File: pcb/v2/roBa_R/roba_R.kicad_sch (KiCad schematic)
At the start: 50 parts, among them J2 Conn_01x01-Connector_Generic, J3 Conn_01x01-Connector_Generic, J4 Conn_01x01-Connector_Generic, J5 Conn_01x01-Connector_Generic, J6 Conn_01x01-Connector_Generic, J7 Conn_01x01-Connector_Generic, SW1 SW_PUSH, SW10 SW_PUSH, SW11 SW_PUSH, SW12 SW_PUSH, SW13 SW_PUSH, SW14 SW_PUSH, SW15 SW_PUSH, SW16 SW_PUSH, SW17 SW_PUSH, SW18 SW_PUSH, SW19 SW_PUSH, SW2 SW_PUSH, SW20 SW_PUSH, SW21 SW_SPDT, SW3 SW_PUSH, SW4 SW_PUSH, SW5 SW_PUSH, SW6 SW_PUSH, SW7 SW_PUSH, SW8 SW_PUSH, SW9 SW_PUSH

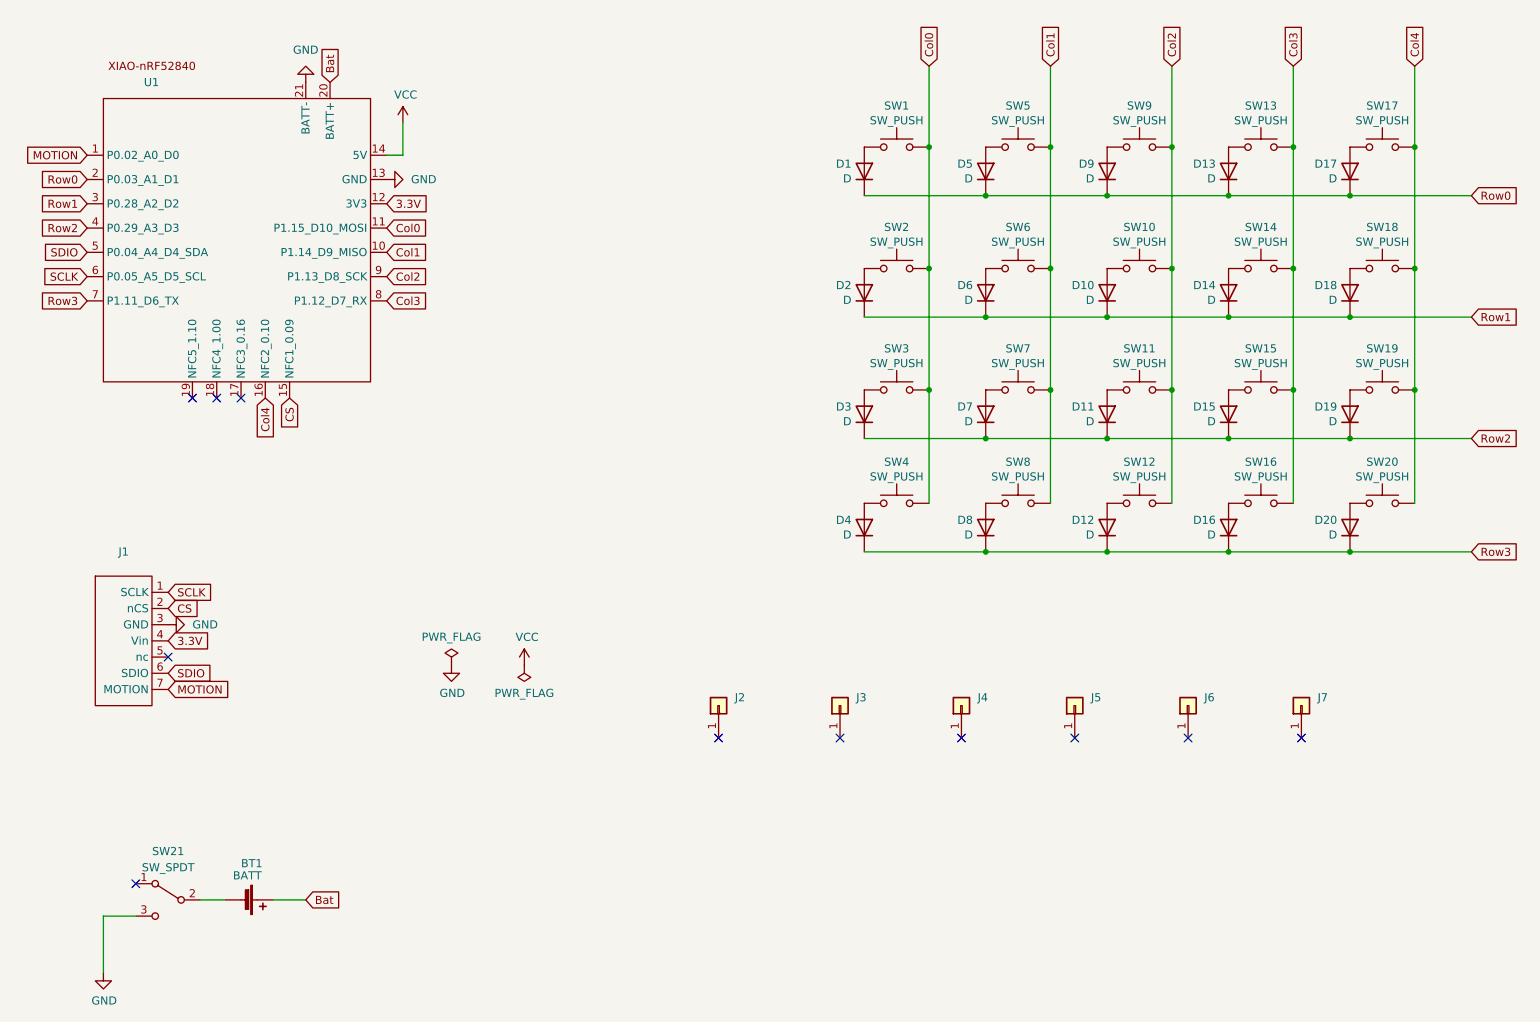
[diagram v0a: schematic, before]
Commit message: Add VIK connector to trackball PCB, Remove earlier revisions
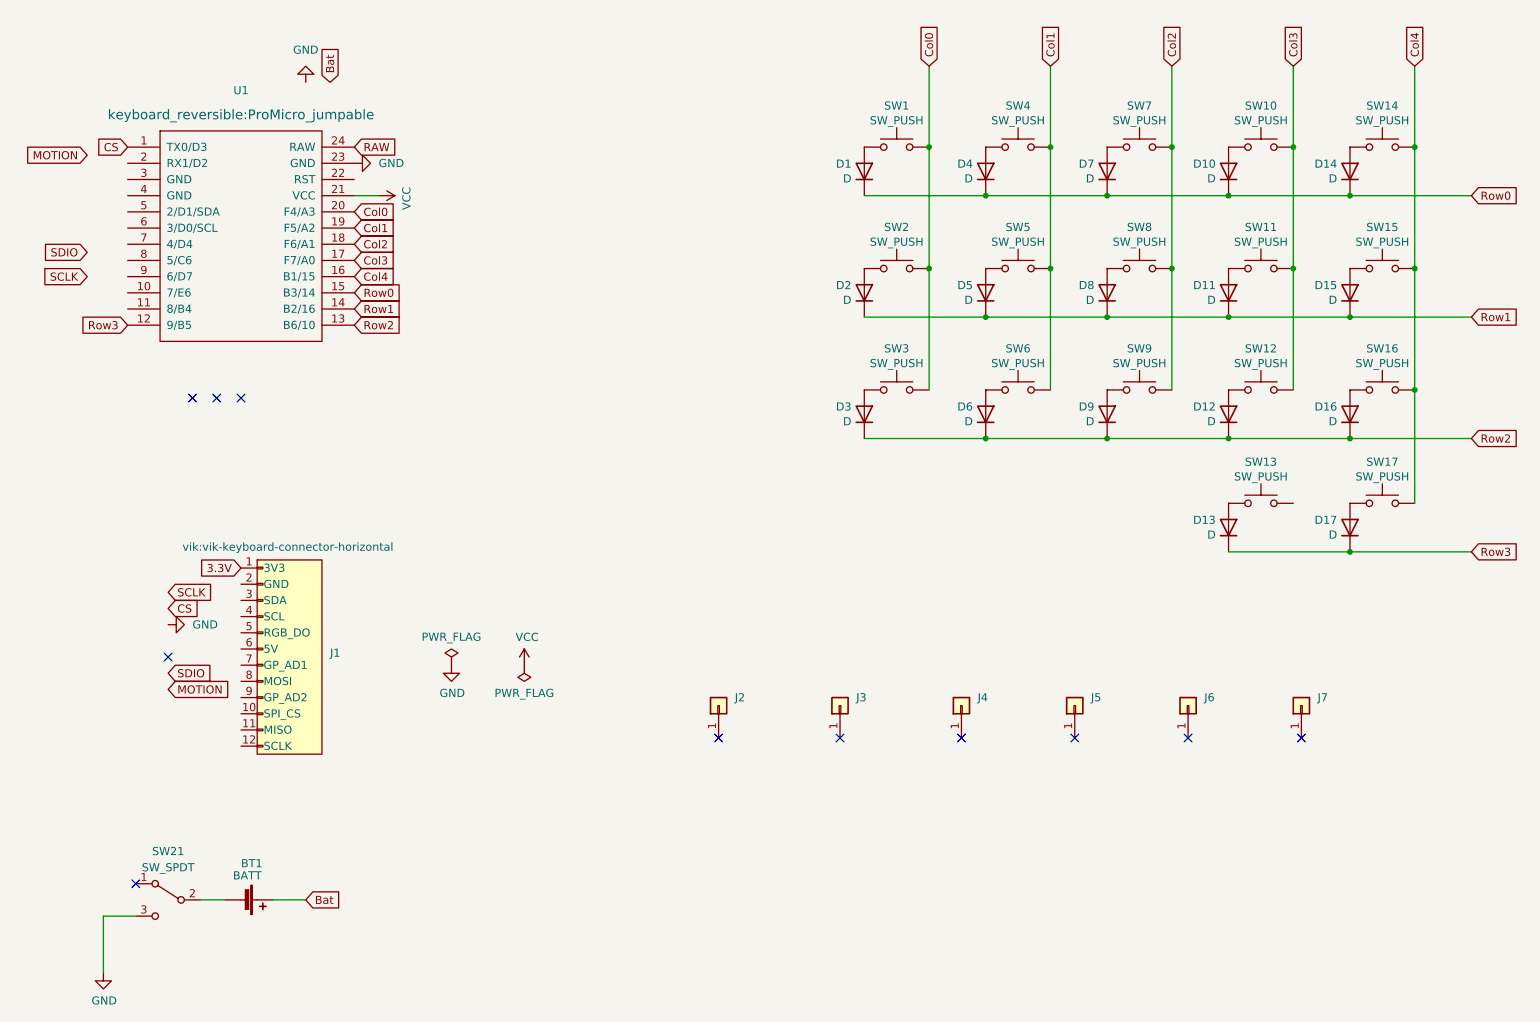
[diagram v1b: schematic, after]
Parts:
- removed D20, D4, D8: D, roBa:Diode_SMD, symbol Device:D
- removed J1: ~, roBa:pmw3610_connector, symbol my:pmw3610_breakout
- removed SW20, SW4, SW8: SW_PUSH, roBa:SW_MX, symbol Switch:SW_Push
- added J1: ~, vik:vik-keyboard-connector-horizontal, symbol vik:vik-keyboard-connector
- U1: footprint roBa:XIAO_nRF52840_wBAT_wNFC_1 -> keyboard_reversible:ProMicro_jumpable; symbol my:XIAO-nRF52840 -> kbd:ProMicro
- renumbered D13 to D10, D14 to D11, D15 to D12, D12 to D13, D17 to D14, D18 to D15, D19 to D16, D16 to D17, D5 to D4, D6 to D5, D7 to D6, D9 to D7, D10 to D8, D11 to D9, SW13 to SW10, SW14 to SW11, SW15 to SW12, SW12 to SW13, SW17 to SW14, SW18 to SW15, SW19 to SW16, SW16 to SW17, SW5 to SW4, SW6 to SW5, SW7 to SW6, SW9 to SW7, SW10 to SW8, SW11 to SW9
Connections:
- net 3.3V: now also J1.1 (3V3); no longer U1.12 (3V3)
- net Bat: no longer U1.20 (BATT+)
- net CS: now also U1.1 (TX0/D3); no longer U1.15 (NFC1_0.09)
- net Col0: now also U1.20 (F4/A3); no longer U1.11 (P1.15_D10_MOSI)
- net Col1: now also U1.19 (F5/A2); no longer U1.10 (P1.14_D9_MISO)
- net Col2: now also U1.18 (F6/A1); no longer SW13.1, U1.9 (P1.13_D8_SCK)
- net Col3: now also U1.17 (F7/A0); no longer SW17.1, U1.8 (P1.12_D7_RX)
- net Col4: now also SW17.1
- net GND: now also U1.23 (GND); no longer U1.13 (GND), U1.21 (BATT-)
- net MOTION: no longer U1.1 (P0.02_A0_D0)
- net Row0: now also U1.15 (B3/14); no longer U1.2 (P0.03_A1_D1)
- net Row1: now also U1.14 (B2/16); no longer U1.3 (P0.28_A2_D2)
- net Row2: now also U1.13 (B6/10); no longer U1.4 (P0.29_A3_D3)
- net Row3: now also U1.12 (9/B5); no longer U1.7 (P1.11_D6_TX)
- net SCLK: no longer U1.6 (P0.05_A5_D5_SCL)
- net SDIO: no longer U1.5 (P0.04_A4_D4_SDA)
- net VCC: now also U1.21 (VCC); no longer U1.14 (5V)
- new net RAW: U1.24 (RAW)
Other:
- moved on the sheet: D13, D17, SW13, SW17
